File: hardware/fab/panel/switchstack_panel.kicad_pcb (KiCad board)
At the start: 4 copper layers, 173.4 x 72.4 mm, 217 parts

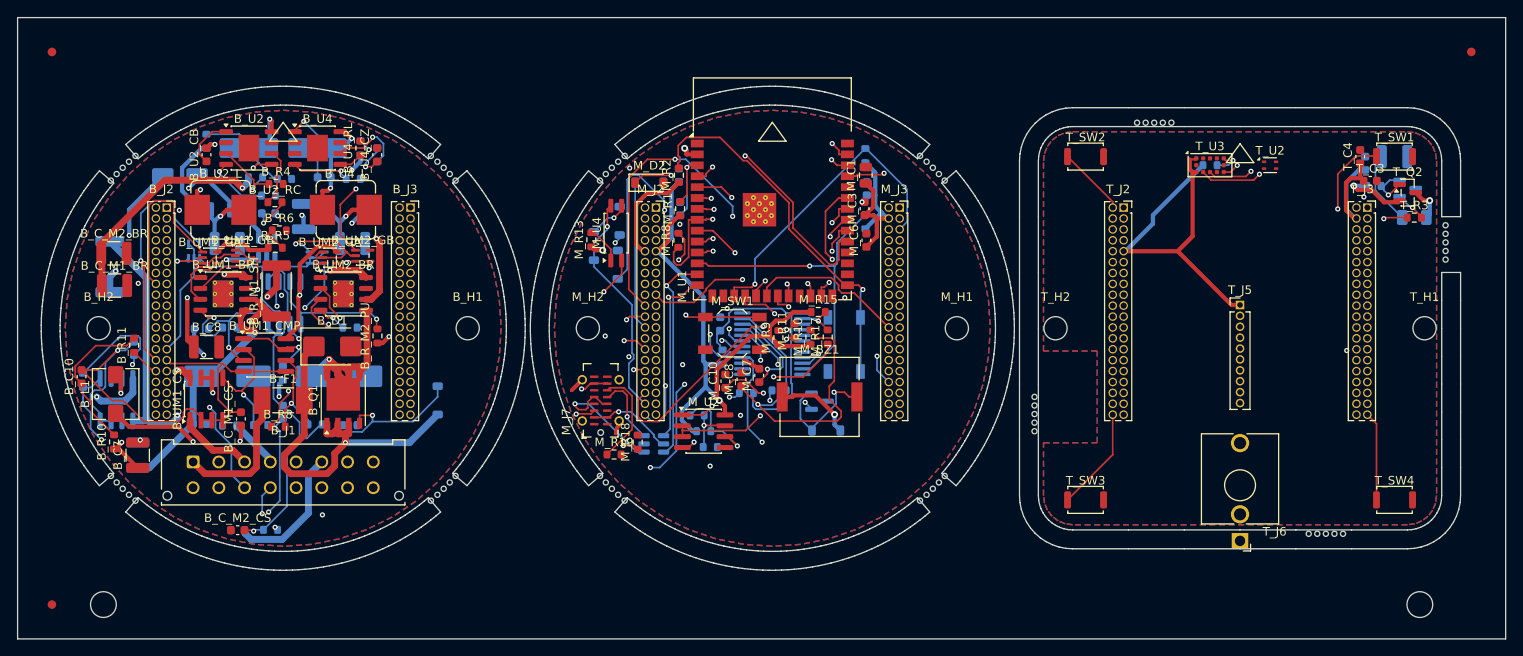
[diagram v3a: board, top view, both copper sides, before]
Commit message: Alle drei Boards kupferfehlerfrei, und die Bilder zeigen endlich die Stecker
ROUTING. Alle drei Platinen haben jetzt null Kupferfehler:

  Top     179 Segmente,  22 Vias,  7 Signale offen  (vorher 11, 2 Fehler)
  Mid     720 Segmente,  74 Vias,  4 Signale offen  (vorher  6)
  Bottom  811 Segmente,  91 Vias,  6 Signale offen  (vorher  8, 6 Fehler)

Top hatte zwei copper_edge_clearance-Fehler an der USB-C-Kerbe: Eine
BTN2-Bahn lief auf In1.Cu quer durch den Ausschnitt. Der Randkeepout des
Routers kannte die Kerbe gar nicht - er bestand aus vier Balken entlang der
Kanten, und die Kerbe schneidet in eine dieser Kanten hinein. Die einzige
Aussparung darin stammte noch von der Klinkenbuchse, die es nicht mehr gibt.
route_boards.py setzt jetzt NOTCH_KEEPOUT.

M1_ISNS AUF BOTTOM IST MIT ABSICHT LEER. Freerouting hatte das analoge
Motorstrom-Messsignal auf F.Cu direkt an die Vergleichsschwelle V_TRIP_LO
gepresst - vier Kurzschluesse, eine Kreuzung, ein Abstandsfehler, alle in
einem Feld von zwei Millimetern. Einzeln herausgeloeste Segmente haben das
Problem nur verschoben: nach jedem Eingriff dieselben zwei Netze an der
naechsten Stelle. Das Netz ist deshalb komplett entfernt und wird von Hand
gezogen. Sachlich ist die Paarung ohnehin die schlechteste denkbare - koppeln
Messsignal und Ausloeseschwelle, verstimmt sich die Hinderniserkennung
selbst, ohne dass eine DRC das je bemerkt. docs/16 erklaert es samt Auflagen.

DIE BILDER ZEIGTEN DIE STECKVERBINDER NICHT - und es lag nicht an den
Modellen. Die Bildkette war nie ein Skript, sondern jedes Mal von Hand
getippt. Dadurch stammten die Teile aus verschiedenen Zeitpunkten: Modelle
16:04, Stapel-STEPs 15:59, Unterseiten-Renderings 13:41. Ausgerechnet die
Unterseiten zeigen den Feldstecker und die USB-Buchse.

tools/render_all.py macht daraus einen Aufruf: sechs Boardansichten, drei
STEP-Ausgaben mit Modellen, das Stapelbild und die Gesamtbaugruppe - ein
Zeitstand fuer alles. Renderings jetzt mit transparentem Hintergrund, damit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
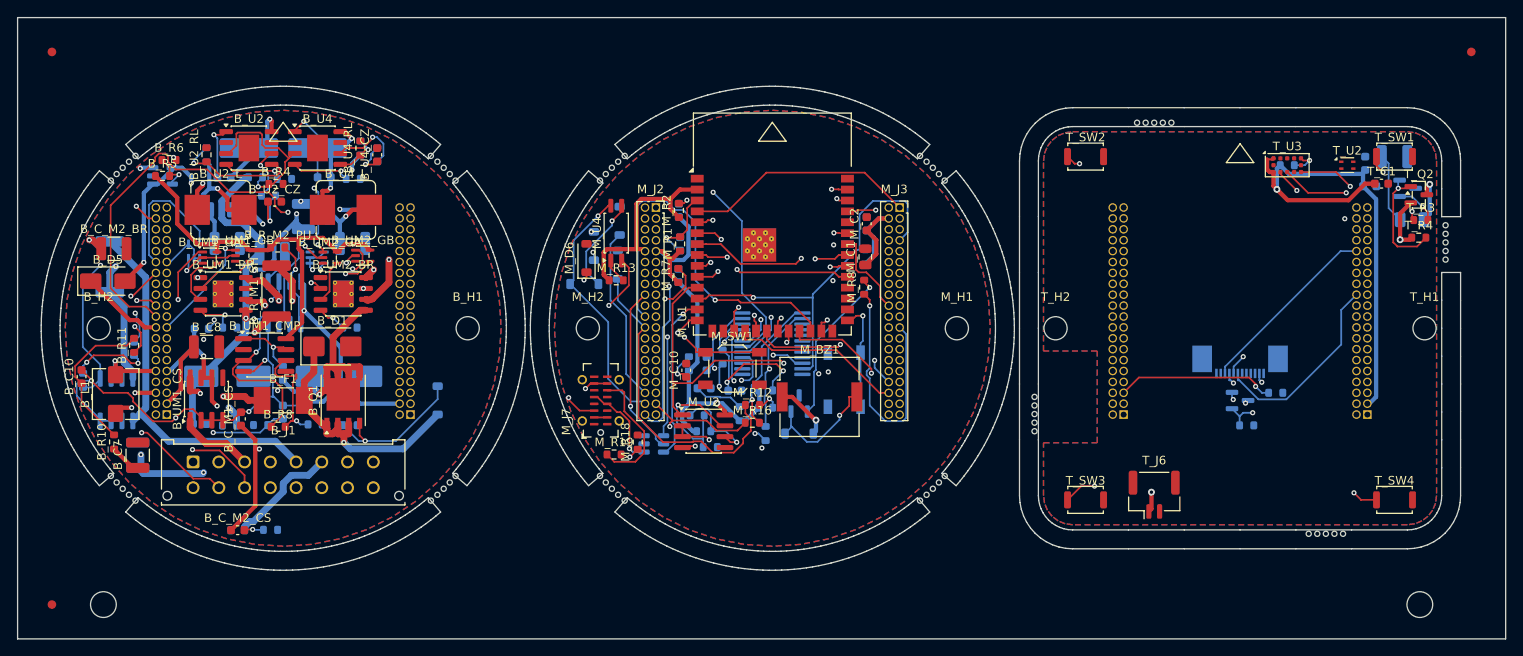
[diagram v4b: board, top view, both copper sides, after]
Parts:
- added T_Q_BL: N-FET 30V 1A, SOT-23, B.Cu at (55.8, 8.42)
- added T_R_BL: 39R, R_0603_1608Metric, B.Cu at (59.9, 7.52)
- added T_R_BLG: 100k, R_0603_1608Metric, B.Cu at (56.5, 11.3)
- B_C_M1_BR, B_J2, B_J3, B_U2_CB, B_U2_RC, M_C3, M_C6, M_C7, M_C8, M_D2, M_R10, M_R11, M_R15, M_R17, M_R9, T_C3, T_C4, T_J2, T_J3: moved to B.Cu
- B_D5, B_U2_CZ, B_U2_RL, M_C2, M_D6, M_R12, M_R16, M_R7, T_C1, T_R4: moved to F.Cu
- T_J5: value ST7789 240x280 -> ER-TFT1.69-3; footprint PinHeader_1x10_P1.27mm_Vertical -> TE_1-1734839-2_1x12-1MP_P0.5mm_Horizontal; moved to B.Cu
- T_J6: value Stern Klinke -> Stern; footprint Jack_3.5mm_QingPu_WQP-PJ398SM_Vertical_CircularHoles -> JST_GH_BM02B-GHS-TBT_1x02-1MP_P1.25mm_Vertical
- moved M_R7 25.9 mm to (-9.70, -6.15)
- moved B_J2 24.1 mm to (-69.3, 10.1)
- moved B_J3 24.1 mm to (-40.9, 10.1)
- moved T_J2 24.1 mm to (42.2, 10.1)
- moved T_J3 24.1 mm to (70.6, 10.1)
- moved M_R8 22.3 mm to (11.9, -4.79)
- moved M_C6 22.3 mm to (-9.70, -6.15)
- moved B_C_M1_BR 18.8 mm to (-57.0, -8.73)
- moved M_R15 16.2 mm to (-8.47, 4.13), turned to 90 degrees
- moved B_R5 15.6 mm to (-69.8, -17.8)
- moved B_R_M2_PU 15.5 mm to (-56.4, -9.41), turned to 0 degrees
- moved B_R6 15.2 mm to (-69.0, -19.6)
- moved B_D5 14.9 mm to (-76.2, -5.49)
- moved B_U3 14.8 mm to (-69.8, -17.8), turned to 0 degrees
- moved M_R17 13.4 mm to (0.47, 12.3)
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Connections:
- T_J5 pad 1: TOP_3V3_SYS -> TOP_DISP_TE
- T_J5 pad 10: TOP_DISP_BL -> TOP_DISP_LEDA
- T_J5 pad 3: TOP_QSPI_CLK -> TOP_QSPI_D1
- T_J5 pad 4: TOP_QSPI_D0 -> TOP_DISP_RST
- T_J5 pad 5: TOP_QSPI_D1 -> TOP_QSPI_D0
- T_J5 pad 6: TOP_QSPI_D2 -> TOP_QSPI_CLK
- T_J5 pad 7: TOP_QSPI_D3 -> TOP_DISP_CS
- T_J5 pad 8: TOP_DISP_CS -> TOP_3V3_SYS
- T_J5 pad 9: TOP_DISP_RST -> TOP_3V3_SYS
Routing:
- net BOT_HOOD_A: track 28.9 -> 69.9 mm, vias 0 -> 1
- net BOT_24V_PROT: track 104.2 -> 142.6 mm, vias 3 -> 5
- net MID_3V3_SYS: track 159.3 -> 124.0 mm, vias 3 -> 1
- net BOT_5V_SYS: track 37.6 -> 71.4 mm, vias 2 -> 4
- net TOP_BTN4: track 10.4 -> 39.4 mm, vias 0 -> 1
- net TOP_BTN3: track 12.1 -> 41.0 mm, vias 0 -> 1
- net TOP_QSPI_D3: track 26.5 -> 0.00 mm
- net MID_RELAY_CTL: track 67.6 -> 42.0 mm, vias 4 -> 2
- net TOP_BTN2: track 8.12 -> 32.6 mm, vias 0 -> 1
- net MID_QSPI_D3: track 0.00 -> 23.4 mm, vias 0 -> 1
- net TOP_DISP_RST: track 21.1 -> 43.6 mm, vias 0 -> 1
- net MID_EXP_P7: track 41.7 -> 19.4 mm, vias 1 -> 2
- net BOT_HOOD_B: track 25.5 -> 47.2 mm
- net BOT_RS485_A: track 39.0 -> 60.7 mm
- net MID_PGND: track 21.0 -> 0.00 mm
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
